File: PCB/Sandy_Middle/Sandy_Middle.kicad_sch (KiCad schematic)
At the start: 73 parts, among them J1 Conn_02x02_Top_Bottom, J2 Conn_02x02_Top_Bottom, J3 Conn_02x02_Top_Bottom

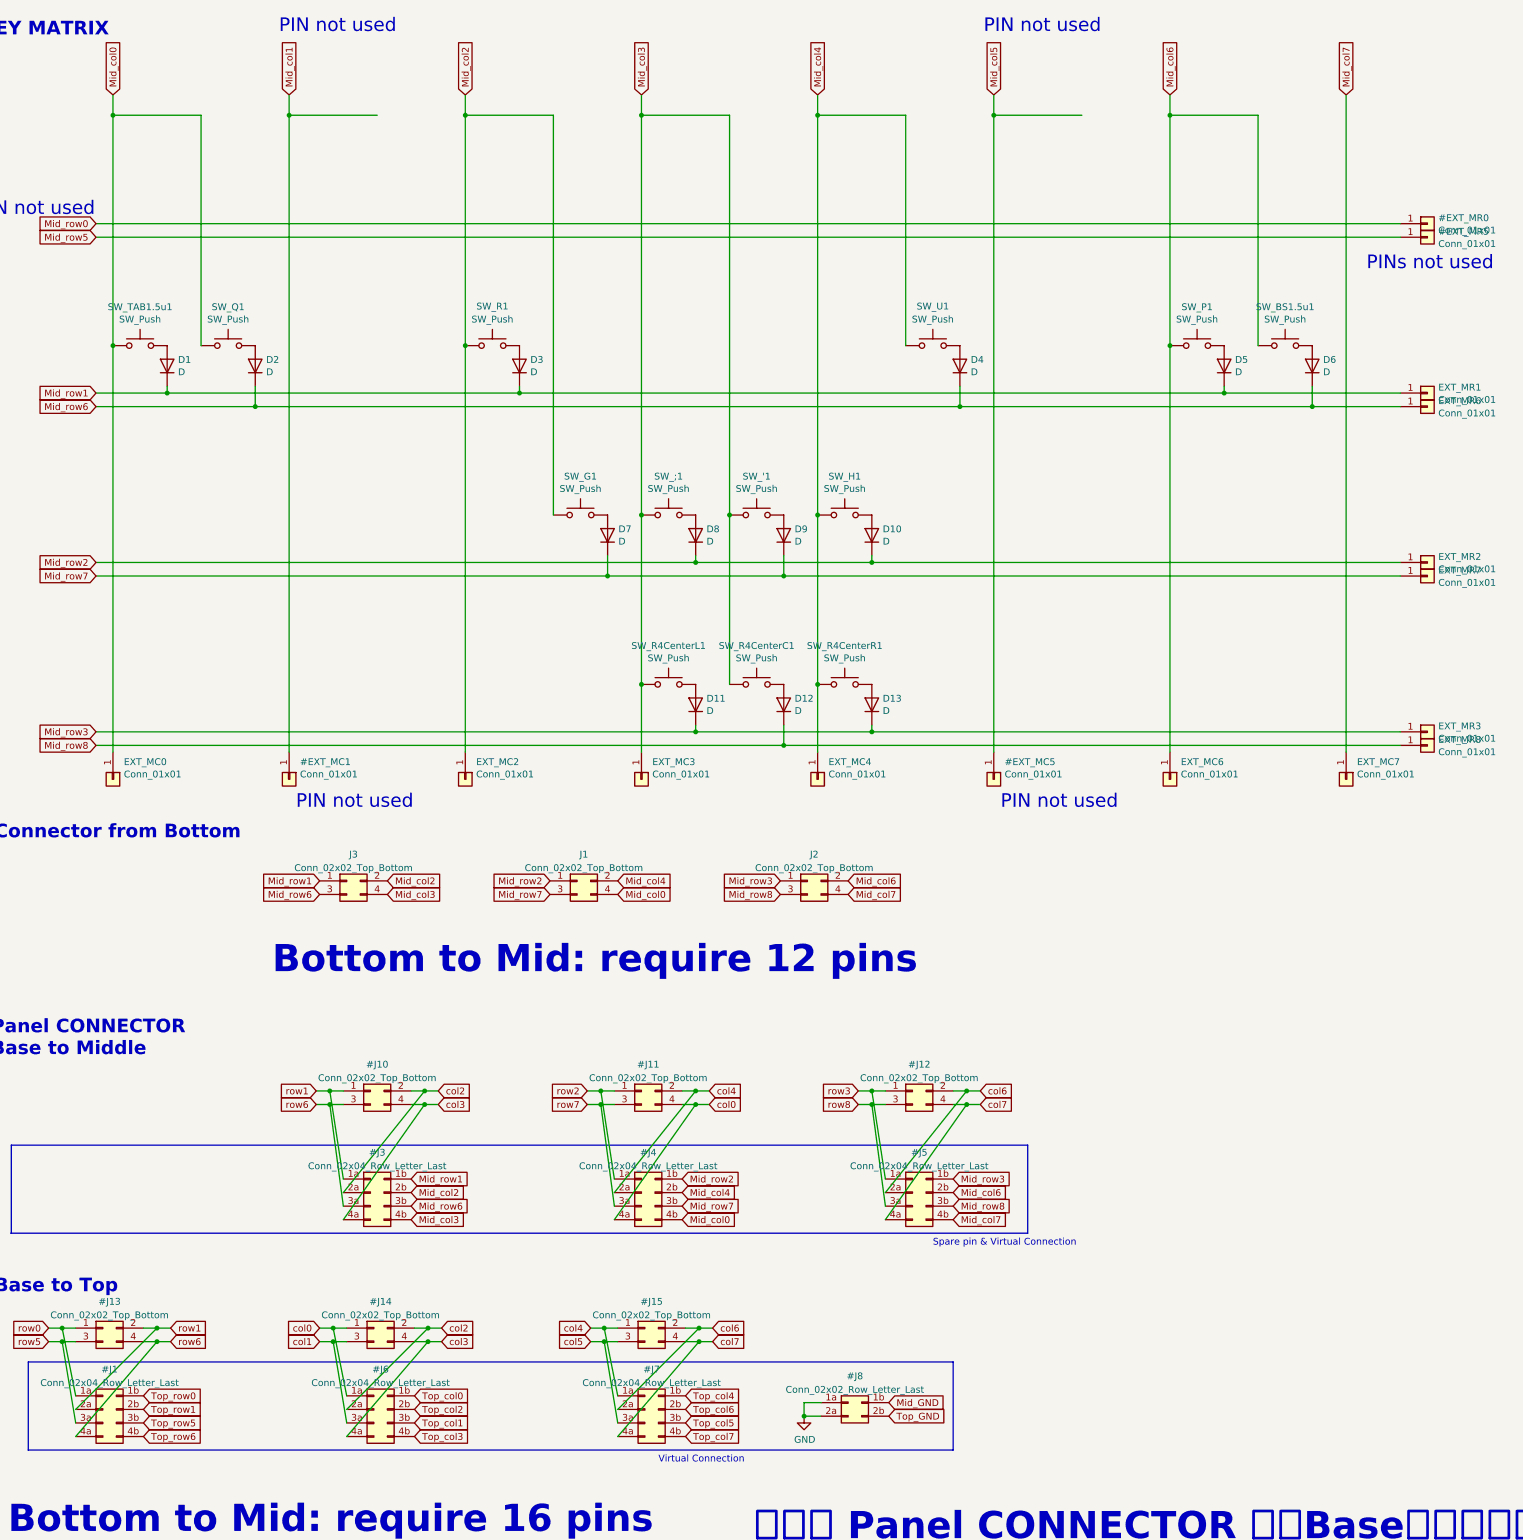
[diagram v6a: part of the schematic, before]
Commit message: スイッチマトリックス更新。COL7を削除してスイッチを再配置。
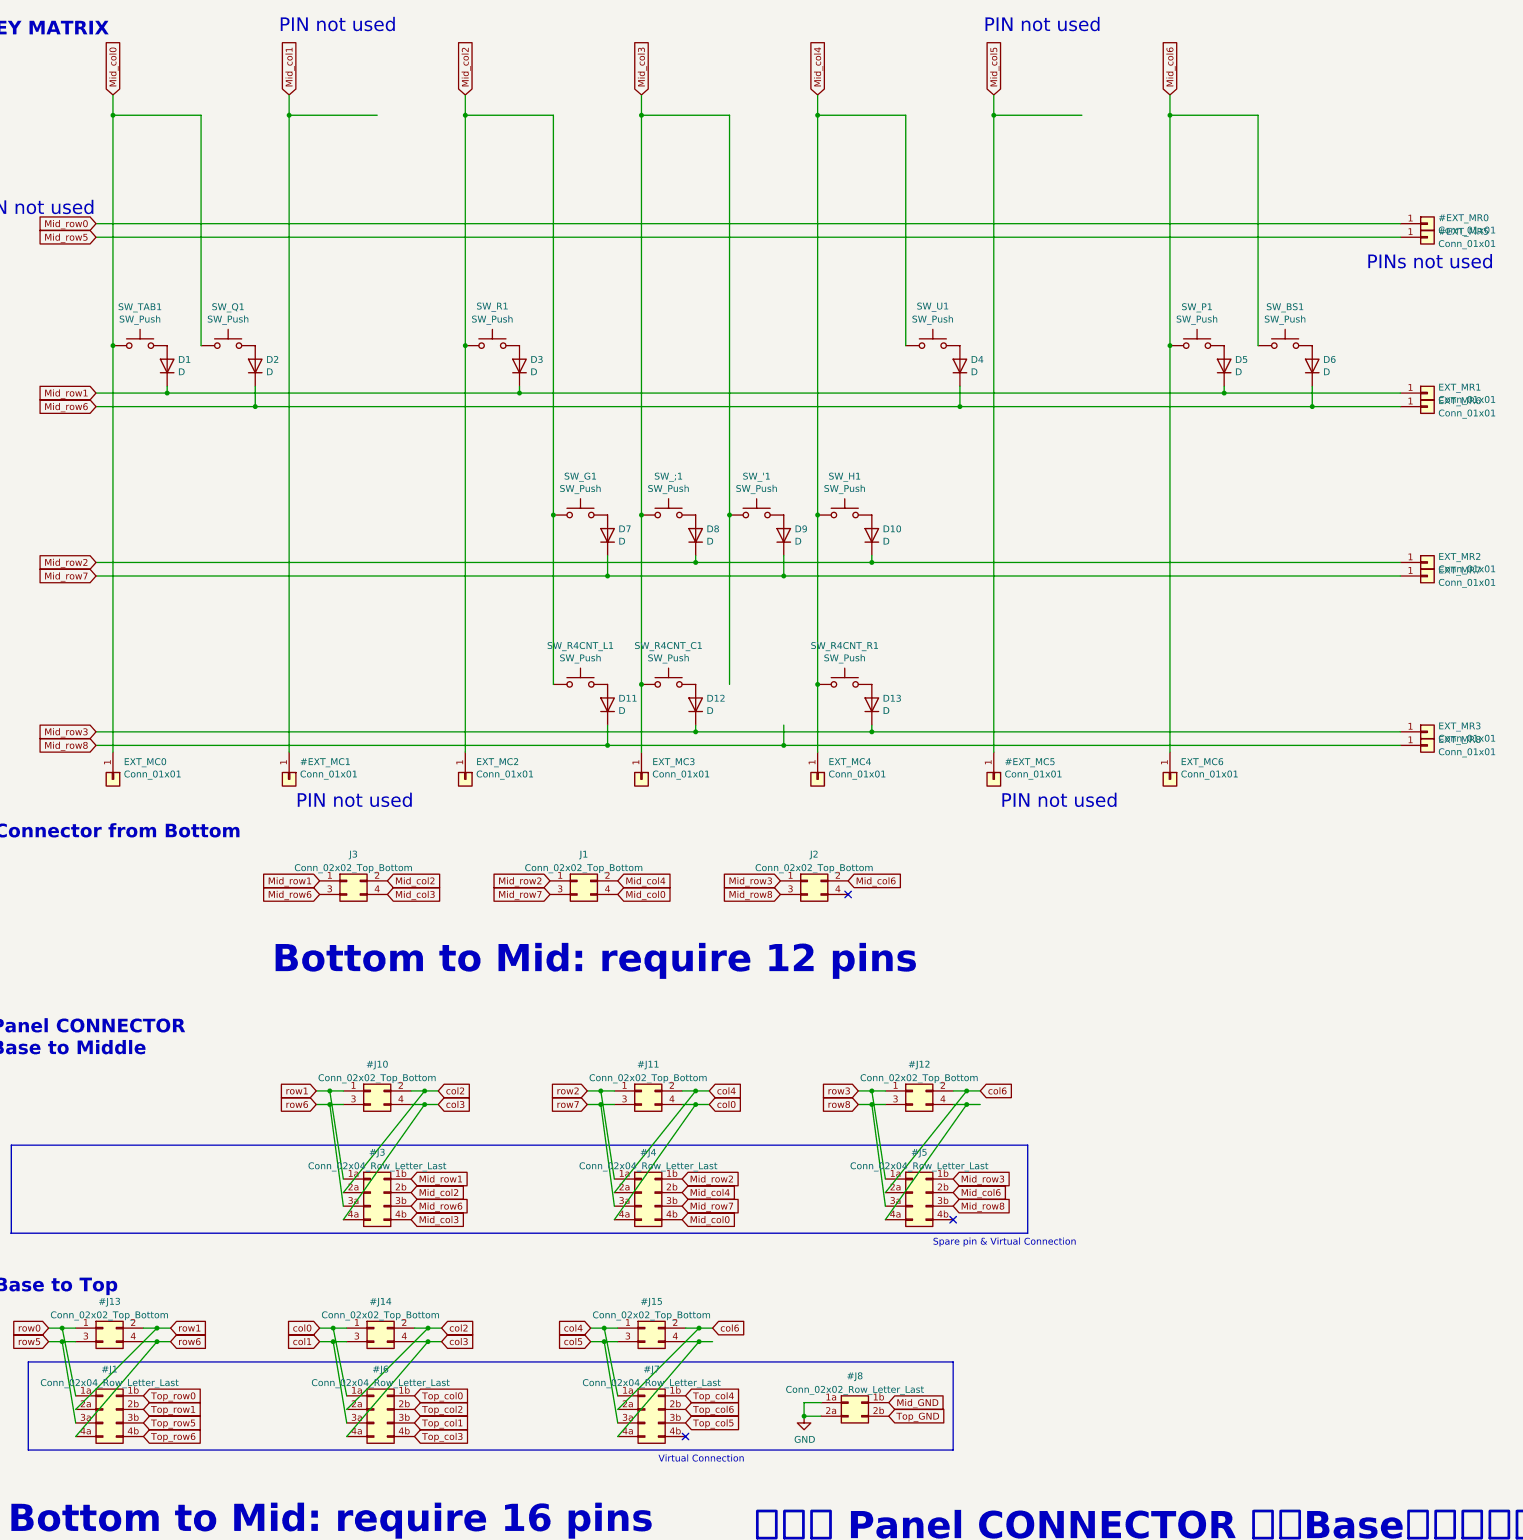
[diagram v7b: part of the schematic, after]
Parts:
- removed EXT_MC7: Conn_01x01, TestPoint:TestPoint_THTPad_D2.0mm_Drill1.0mm, symbol Connector_Generic:Conn_01x01
- renumbered SW_BS1.5u1 to SW_BS1, SW_R4CenterC1 to SW_R4CNT_C1, SW_R4CenterL1 to SW_R4CNT_L1, SW_R4CenterR1 to SW_R4CNT_R1, SW_TAB1.5u1 to SW_TAB1
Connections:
- net Mid_col2: now also SW_R4CNT_L1.1
- net Mid_col3: no longer SW_R4CNT_L1.1
- net Mid_row3: now also D12.1 (K); no longer D11.1 (K)
- net Mid_row8: now also D11.1 (K); no longer D12.1 (K)
- net Mid_col7: no longer names the net of #J5.4b (Pin_4b)
- net Mid_col7: no longer J2.4 (Pin_4)
- net Top_col7: no longer names the net of #J7.4b (Pin_4b)
- net col7: no longer names the net of #J12.4 (Pin_4), #J5.4a (Pin_4a)
- net col7: no longer #J15.4 (Pin_4), #J7.4a (Pin_4a)
- new net: #J15.4 (Pin_4), #J7.4a (Pin_4a)
- no-connect marks 0 -> 3
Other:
- moved on the sheet: D11, D12, SW_R4CNT_C1, SW_R4CNT_L1
